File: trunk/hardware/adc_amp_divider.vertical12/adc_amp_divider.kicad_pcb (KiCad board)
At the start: 2 copper layers, 66 x 97.2 mm, 120 parts, among them M200 CONN_1, M201 CONN_1, M202 CONN_1, P201 CONN_10X2, P202 CONN_3, P203 CONN_2, P204 CONN_1, P205 CONN_1, P207 CONN_2, P208 CONN_6, P209 CONN_6, U201 LMV324IDR, U202 LMV324IDR, U203 LMV324IDR

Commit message: improvements in the left-bottom corner
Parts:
- moved M200 3.51 mm to (122.9, 158.9)
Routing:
- net /OUT5: track 34.9 -> 38.6 mm, vias 0 -> 2
- net /OUT6: track 45.4 -> 48.7 mm
- net /OUT1: track 11.1 -> 12.1 mm
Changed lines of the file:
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@@
     (thickness 1.6)
     (drawings 17)
-    (tracks 1024)
+    (tracks 1035)
     (zones 0)
     (modules 120)
@@
   )
   (module PIN_ARRAY_1 (layer F.Cu)
-    (at 123.698 155.448 90)
+    (at 122.936 158.877 90)
     (descr "1 pin")
     (tags "CONN DEV")
@@
   (segment (start 132.588 155.7655) (end 132.2705 155.7655) (width 0.254) (layer F.Cu) (net 14) (status 30))
   (segment (start 128.27 151.13) (end 127 149.86) (width 0.254) (layer F.Cu) (net 14) (status 20))
-  (segment (start 128.27 151.765) (end 128.27 151.13) (width 0.254) (layer F.Cu) (net 14))
-  (segment (start 132.2705 155.7655) (end 128.27 151.765) (width 0.254) (layer F.Cu) (net 14) (status 10))
+  (segment (start 128.27 153.67) (end 128.27 151.13) (width 0.254) (layer F.Cu) (net 14))
+  (segment (start 132.2705 155.7655) (end 130.302 153.797) (width 0.254) (layer F.Cu) (net 14) (status 10))
+  (segment (start 130.302 153.797) (end 128.27 153.67) (width 0.254) (layer F.Cu) (net 14) (status 10))
   (segment (start 135.255 155.7655) (end 132.588 155.7655) (width 0.254) (layer F.Cu) (net 14) (status 30))
   (segment (start 165.862 154.2415) (end 165.862 157.099) (width 0.254) (layer F.Cu) (net 15))
@@
   (segment (start 140.589 148.5265) (end 138.049 148.5265) (width 0.254) (layer F.Cu) (net 20) (status 30))
   (segment (start 138.049 148.5265) (end 137.922 148.3995) (width 0.254) (layer F.Cu) (net 20) (status 30))
+  (segment (start 125.73 154.178) (end 125.73 156.21) (width 0.254) (layer B.Cu) (net 21))
+  (segment (start 125.73 156.21) (end 130.302 156.21) (width 0.254) (layer B.Cu) (net 21))
+  (via (at 125.73 154.178) (size 0.889) (layers F.Cu B.Cu) (net 21))
+  (segment (start 130.302 156.21) (end 131.064 155.829) (width 0.254) (layer B.Cu) (net 21))
+  (via (at 131.064 155.829) (size 0.889) (layers F.Cu B.Cu) (net 21))
+  (segment (start 131.185209 155.950209) (end 131.064 155.829) (width 0.254) (layer F.Cu) (net 21))
+  (segment (start 131.710582 156.972) (end 131.185209 155.950209) (width 0.254) (layer F.Cu) (net 21))
+  (segment (start 145.923 155.8925) (end 144.8435 156.972) (width 0.254) (layer F.Cu) (net 21) (status 10))
   (segment (start 144.8435 156.972) (end 131.710582 156.972) (width 0.254) (layer F.Cu) (net 21))
+  (segment (start 131.185209 155.834791) (end 131.069791 155.834791) (width 0.254) (layer B.Cu) (net 21))
+  (segment (start 131.069791 155.834791) (end 131.064 155.829) (width 0.254) (layer B.Cu) (net 21))
   (segment (start 128.905 144.78) (end 127.635 146.05) (width 0.254) (layer F.Cu) (net 21) (status 10))
   (segment (start 127.635 146.05) (end 126.492 146.05) (width 0.254) (layer F.Cu) (net 21))
   (segment (start 126.492 146.05) (end 125.603 146.939) (width 0.254) (layer F.Cu) (net 21))
-  (segment (start 125.603 146.939) (end 125.603 150.864418) (width 0.254) (layer F.Cu) (net 21))
-  (segment (start 145.923 155.8925) (end 144.8435 156.972) (width 0.254) (layer F.Cu) (net 21) (status 10))
+  (segment (start 125.603 146.939) (end 125.73 154.178) (width 0.254) (layer F.Cu) (net 21))
+  (segment (start 125.73 154.178) (end 125.73 154.293418) (width 0.254) (layer F.Cu) (net 21))
   (segment (start 128.905 144.78) (end 129.54 144.78) (width 0.254) (layer F.Cu) (net 21) (status 30))
-  (segment (start 131.710582 156.972) (end 125.603 150.864418) (width 0.254) (layer F.Cu) (net 21))
   (segment (start 148.717 155.7655) (end 146.05 155.7655) (width 0.254) (layer F.Cu) (net 21) (status 30))
   (segment (start 146.05 155.7655) (end 145.923 155.8925) (width 0.254) (layer F.Cu) (net 21) (status 30))
@@
   (segment (start 151.638 157.48) (end 152.654 156.464) (width 0.254) (layer F.Cu) (net 22))
   (segment (start 131.572 157.48) (end 151.638 157.48) (width 0.254) (layer F.Cu) (net 22))
-  (segment (start 125.095 151.003) (end 131.572 157.48) (width 0.254) (layer F.Cu) (net 22))
-  (segment (start 125.095 146.685) (end 125.095 151.003) (width 0.254) (layer F.Cu) (net 22))
-  (segment (start 125.73 146.05) (end 125.095 146.685) (width 0.254) (layer F.Cu) (net 22))
+  (segment (start 124.841 156.083) (end 130.048 156.21) (width 0.254) (layer F.Cu) (net 22))
+  (segment (start 130.048 156.21) (end 131.572 157.48) (width 0.254) (layer F.Cu) (net 22))
+  (segment (start 124.841 146.685) (end 124.841 156.083) (width 0.254) (layer F.Cu) (net 22))
+  (segment (start 125.73 146.05) (end 124.841 146.685) (width 0.254) (layer F.Cu) (net 22))
   (segment (start 125.73 144.272) (end 125.73 146.05) (width 0.254) (layer F.Cu) (net 22))
   (segment (start 127 143.002) (end 125.73 144.272) (width 0.254) (layer F.Cu) (net 22) (status 10))

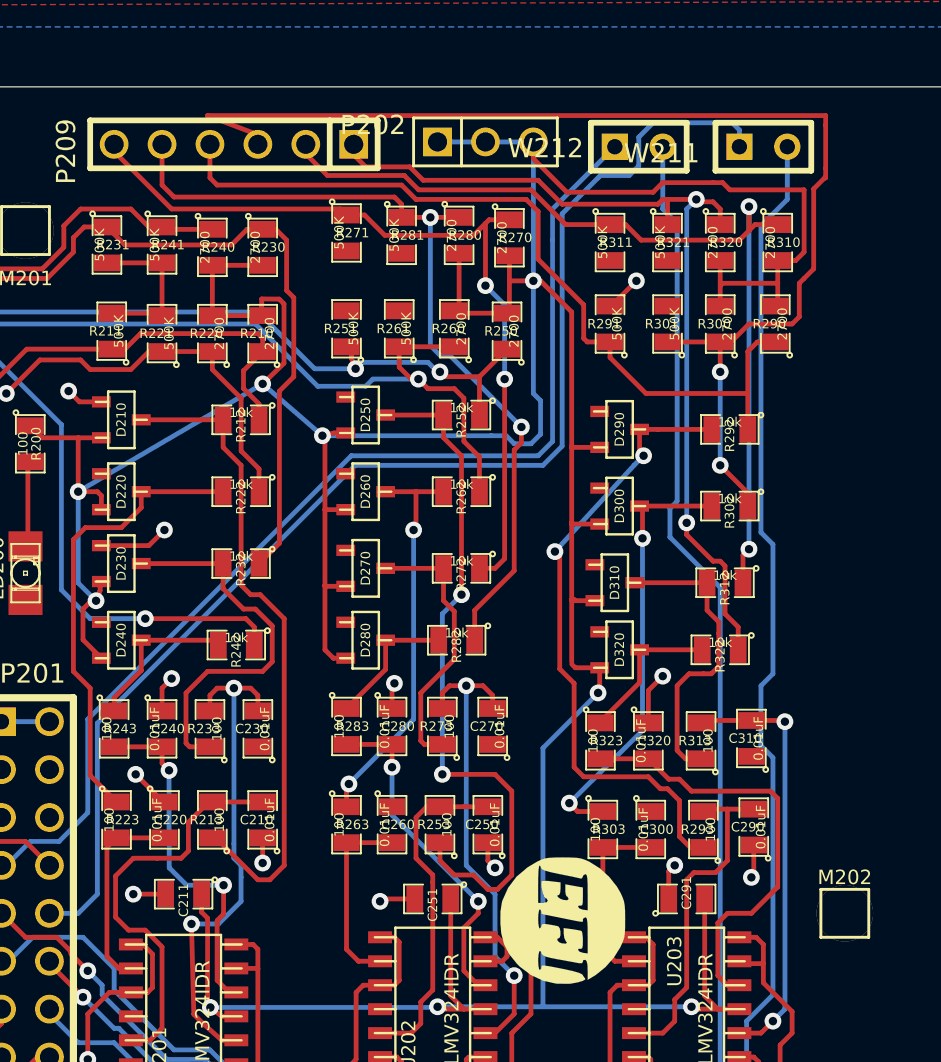
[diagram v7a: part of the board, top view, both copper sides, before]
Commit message: some track improvements
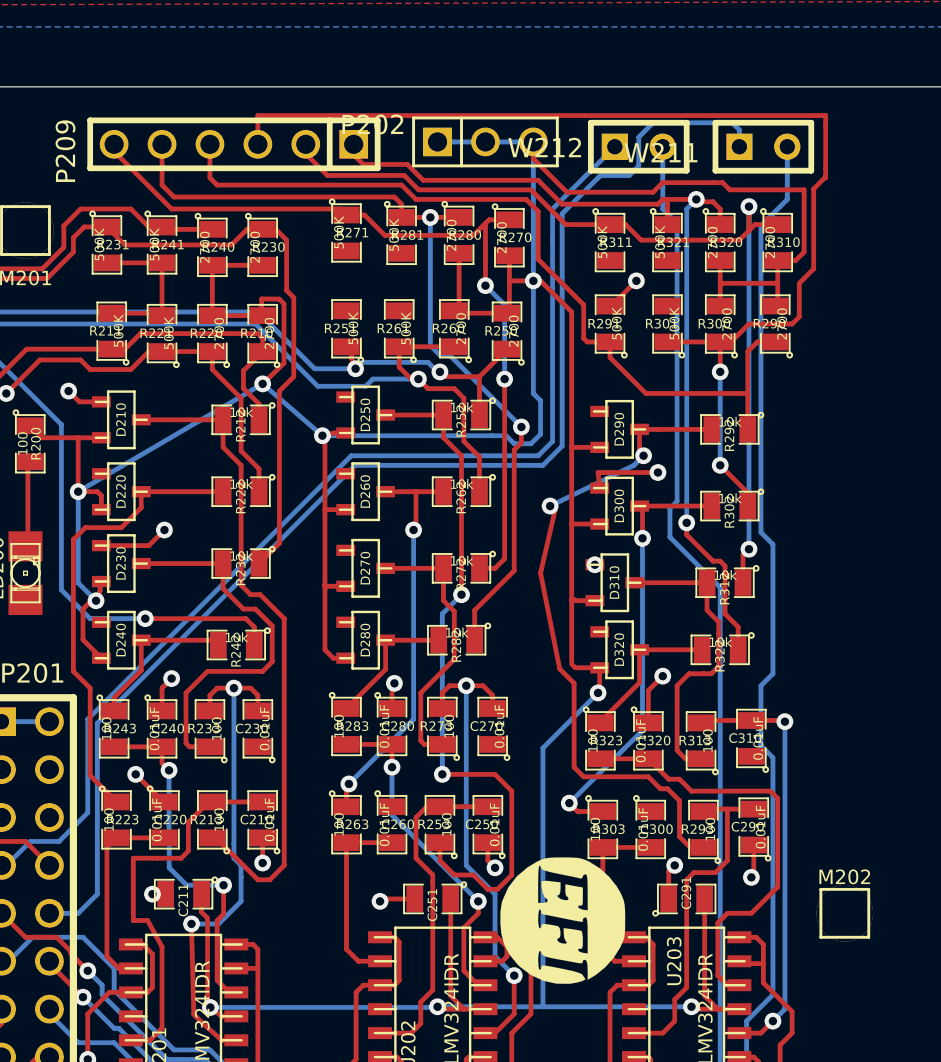
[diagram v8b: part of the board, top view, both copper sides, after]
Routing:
- net /INP10: track 64.2 -> 59.7 mm
- net GND: track 54.8 -> 57.8 mm, vias 15 -> 17
- net N-0000023: track 34.2 -> 35.5 mm
- net N-0000084: track 21.8 -> 20.9 mm
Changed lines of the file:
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@@
     (thickness 1.6)
     (drawings 17)
-    (tracks 1035)
+    (tracks 1044)
     (zones 0)
     (modules 120)
@@
   (segment (start 166.624 105.918) (end 168.783 105.918) (width 0.254) (layer F.Cu) (net 3))
   (segment (start 165.1 106.8705) (end 165.6715 106.8705) (width 0.254) (layer F.Cu) (net 3))
-  (segment (start 140.589 95.885) (end 137.922 94.869) (width 0.254) (layer F.Cu) (net 3))
-  (segment (start 137.922 94.869) (end 170.688 94.869) (width 0.254) (layer F.Cu) (net 3))
+  (segment (start 140.589 95.885) (end 140.589 94.869) (width 0.254) (layer F.Cu) (net 3))
+  (segment (start 140.589 94.869) (end 170.688 94.869) (width 0.254) (layer F.Cu) (net 3))
   (segment (start 170.688 94.869) (end 170.688 95.377) (width 0.254) (layer F.Cu) (net 3))
   (segment (start 170.688 95.377) (end 170.688 97.663) (width 0.254) (layer F.Cu) (net 3))
@@
   (segment (start 163.83 99.314) (end 162.306 99.314) (width 0.254) (layer F.Cu) (net 5))
   (segment (start 162.306 99.314) (end 162.052 99.314) (width 0.254) (layer F.Cu) (net 5))
-  (segment (start 145.669 96.951798) (end 146.304 97.586798) (width 0.254) (layer F.Cu) (net 5))
-  (segment (start 146.304 97.586798) (end 148.640798 97.586798) (width 0.254) (layer F.Cu) (net 5))
-  (segment (start 148.640798 97.586798) (end 149.352 98.298) (width 0.254) (layer F.Cu) (net 5))
+  (segment (start 145.669 96.951798) (end 146.177 97.459798) (width 0.254) (layer F.Cu) (net 5))
+  (segment (start 146.177 97.459798) (end 148.513798 97.459798) (width 0.254) (layer F.Cu) (net 5))
+  (segment (start 148.513798 97.459798) (end 149.352 98.298) (width 0.254) (layer F.Cu) (net 5))
   (segment (start 149.352 98.298) (end 155.448 98.298) (width 0.254) (layer F.Cu) (net 5))
   (segment (start 155.448 98.298) (end 156.718 99.568) (width 0.254) (layer F.Cu) (net 5))
@@
   (segment (start 123.063 133.35) (end 128.27 133.35) (width 0.254) (layer F.Cu) (net 27) (status 10))
   (segment (start 128.27 133.35) (end 129.54 134.62) (width 0.254) (layer F.Cu) (net 27) (status 20))
+  (via (at 158.45536 118.6815) (size 0.889) (layers F.Cu B.Cu) (net 28))
+  (segment (start 158.496 118.618) (end 158.496 118.64086) (width 0.254) (layer B.Cu) (net 28))
+  (segment (start 158.496 118.64086) (end 158.45536 118.6815) (width 0.254) (layer B.Cu) (net 28))
+  (segment (start 158.623 113.792) (end 161.163 113.792) (width 0.254) (layer F.Cu) (net 28))
+  (segment (start 158.70936 114.51336) (end 158.623 113.792) (width 0.254) (layer F.Cu) (net 28))
+  (segment (start 158.70936 114.6175) (end 158.70936 114.51336) (width 0.254) (layer F.Cu) (net 28))
+  (via (at 161.798 113.792) (size 0.889) (layers F.Cu B.Cu) (net 28))
+  (segment (start 161.163 113.792) (end 161.798 113.792) (width 0.254) (layer F.Cu) (net 28))
   (segment (start 132.29336 110.0455) (end 131.1275 110.0455) (width 0.254) (layer F.Cu) (net 28))
   (via (at 130.556 109.474) (size 0.889) (layers F.Cu B.Cu) (net 28))
@@
   (via (at 147.066 136.525) (size 0.889) (layers F.Cu B.Cu) (net 28))
   (segment (start 147.193 136.398) (end 147.066 136.525) (width 0.254) (layer F.Cu) (net 28))
-  (segment (start 135.6995 136.144) (end 133.985 136.144) (width 0.254) (layer F.Cu) (net 28))
-  (via (at 133.985 136.144) (size 0.889) (layers F.Cu B.Cu) (net 28))
+  (segment (start 135.6995 136.144) (end 135.001 136.144) (width 0.254) (layer F.Cu) (net 28))
+  (via (at 135.001 136.144) (size 0.889) (layers F.Cu B.Cu) (net 28))
   (segment (start 140.843 133.1595) (end 140.843 134.493) (width 0.254) (layer F.Cu) (net 28))
   (via (at 140.843 134.493) (size 0.889) (layers F.Cu B.Cu) (net 28))
@@
   (segment (start 148.209 145.034) (end 148.209 145.923) (width 0.254) (layer F.Cu) (net 36))
   (segment (start 147.955 144.78) (end 148.209 145.034) (width 0.254) (layer F.Cu) (net 36))
-  (segment (start 156.591 118.237) (end 156.591 124.206) (width 0.254) (layer F.Cu) (net 37))
+  (segment (start 156.337 115.824) (end 155.575 119.126) (width 0.254) (layer F.Cu) (net 37))
+  (segment (start 155.575 119.126) (end 156.591 124.206) (width 0.254) (layer F.Cu) (net 37))
   (segment (start 163.5125 133.6675) (end 164.211 133.6675) (width 0.254) (layer F.Cu) (net 37))
   (segment (start 157.353 124.968) (end 156.591 124.206) (width 0.254) (layer F.Cu) (net 37))
@@
   (segment (start 162.941 133.096) (end 162.941 131.191) (width 0.254) (layer F.Cu) (net 37))
   (segment (start 163.5125 133.6675) (end 162.941 133.096) (width 0.254) (layer F.Cu) (net 37))
-  (segment (start 156.591 118.237) (end 156.337 117.983) (width 0.254) (layer F.Cu) (net 37))
+  (segment (start 156.337 115.824) (end 156.083 115.57) (width 0.254) (layer F.Cu) (net 37))
   (segment (start 160.82264 111.506) (end 160.82264 112.68964) (width 0.254) (layer F.Cu) (net 37))
-  (segment (start 156.337 117.983) (end 156.591 118.237) (width 0.254) (layer F.Cu) (net 37))
-  (via (at 156.337 117.983) (size 0.889) (layers F.Cu B.Cu) (net 37))
-  (segment (start 160.528 113.411) (end 156.337 117.983) (width 0.254) (layer B.Cu) (net 37))
+  (segment (start 156.083 115.57) (end 156.337 115.824) (width 0.254) (layer F.Cu) (net 37))
+  (via (at 156.083 115.57) (size 0.889) (layers F.Cu B.Cu) (net 37))
+  (segment (start 160.528 113.411) (end 156.083 115.57) (width 0.254) (layer B.Cu) (net 37))
   (segment (start 161.036 112.903) (end 160.528 113.411) (width 0.254) (layer B.Cu) (net 37))
   (via (at 161.036 112.903) (size 0.889) (layers F.Cu B.Cu) (net 37))
@@
   (segment (start 133.223 140.081) (end 132.588 139.446) (width 0.254) (layer F.Cu) (net 61) (status 10))
   (segment (start 135.636 133.1595) (end 133.096 133.1595) (width 0.254) (layer F.Cu) (net 61) (status 30))
-  (segment (start 135.255 134.239) (end 133.985 134.239) (width 0.254) (layer F.Cu) (net 62))
-  (segment (start 136.525 134.239) (end 135.255 134.239) (width 0.254) (layer F.Cu) (net 62))
-  (segment (start 137.9855 131.2545) (end 136.906 132.334) (width 0.254) (layer F.Cu) (net 62) (status 10))
-  (segment (start 136.906 132.334) (end 136.906 133.858) (width 0.254) (layer F.Cu) (net 62))
-  (segment (start 136.906 133.858) (end 136.525 134.239) (width 0.254) (layer F.Cu) (net 62))
-  (segment (start 138.176 131.2545) (end 137.9855 131.2545) (width 0.254) (layer F.Cu) (net 62) (status 30))
-  (segment (start 134.874 143.891) (end 133.858 143.891) (width 0.254) (layer F.Cu) (net 62))
-  (segment (start 135.509 143.256) (end 134.874 143.891) (width 0.254) (layer F.Cu) (net 62))
+  (segment (start 133.985 137.541) (end 133.985 137.541) (width 0.254) (layer F.Cu) (net 62))
+  (segment (start 133.985 134.239) (end 133.985 137.541) (width 0.254) (layer F.Cu) (net 62))
+  (segment (start 133.985 137.541) (end 133.985 137.541) (width 0.254) (layer F.Cu) (net 62))
+  (segment (start 133.985 137.541) (end 134.747 137.541) (width 0.254) (layer F.Cu) (net 62))
+  (segment (start 134.747 137.541) (end 135.509 138.938) (width 0.254) (layer F.Cu) (net 62))
   (segment (start 135.509 138.938) (end 135.509 143.256) (width 0.254) (layer F.Cu) (net 62))
-  (segment (start 134.62 138.049) (end 135.509 138.938) (width 0.254) (layer F.Cu) (net 62))
-  (segment (start 133.731 138.049) (end 134.62 138.049) (width 0.254) (layer F.Cu) (net 62))
-  (segment (start 133.045202 137.363202) (end 133.731 138.049) (width 0.254) (layer F.Cu) (net 62))
-  (segment (start 133.045202 135.178798) (end 133.045202 137.363202) (width 0.254) (layer F.Cu) (net 62))
-  (segment (start 133.985 134.239) (end 133.045202 135.178798) (width 0.254) (layer F.Cu) (net 62))
+  (segment (start 135.509 143.256) (end 134.874 143.891) (width 0.254) (layer F.Cu) (net 62))
+  (segment (start 134.874 143.891) (end 133.858 143.891) (width 0.254) (layer F.Cu) (net 62))
+  (segment (start 138.176 131.2545) (end 137.9855 131.2545) (width 0.254) (layer F.Cu) (net 62) (status 30))
+  (segment (start 136.906 133.858) (end 136.525 134.239) (width 0.254) (layer F.Cu) (net 62))
+  (segment (start 136.906 132.334) (end 136.906 133.858) (width 0.254) (layer F.Cu) (net 62))
+  (segment (start 137.9855 131.2545) (end 136.906 132.334) (width 0.254) (layer F.Cu) (net 62) (status 10))
+  (segment (start 136.525 134.239) (end 135.255 134.239) (width 0.254) (layer F.Cu) (net 62))
+  (segment (start 135.255 134.239) (end 133.985 134.239) (width 0.254) (layer F.Cu) (net 62))
   (segment (start 140.843 131.2545) (end 138.176 131.2545) (width 0.254) (layer F.Cu) (net 62) (status 30))
   (segment (start 149.733 154.94) (end 144.907 154.94) (width 0.254) (layer F.Cu) (net 63))
